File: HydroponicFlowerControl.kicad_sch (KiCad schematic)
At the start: 0 parts

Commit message: Add title to all schematics pages
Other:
- title: (none) -> RootMaster
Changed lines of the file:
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@@
 	(paper "A4")
 	(title_block
+		(title "RootMaster")
 		(rev "1")
 	)

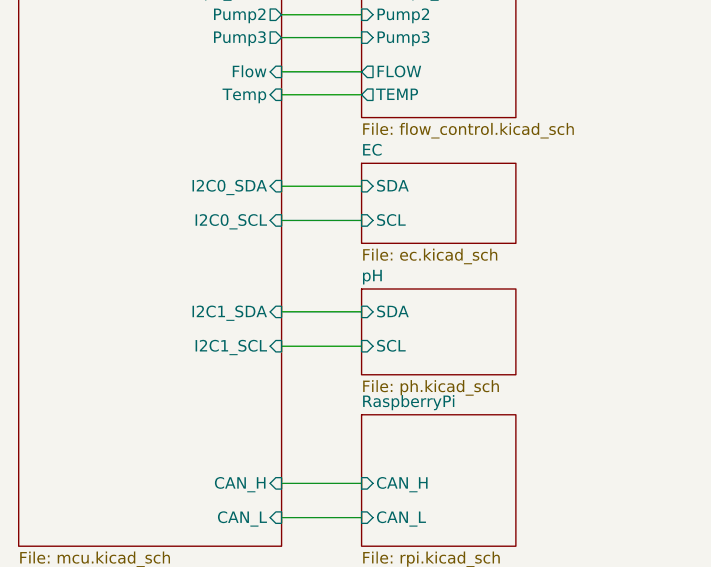
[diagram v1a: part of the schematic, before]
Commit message: Add disable signals for ec and ph
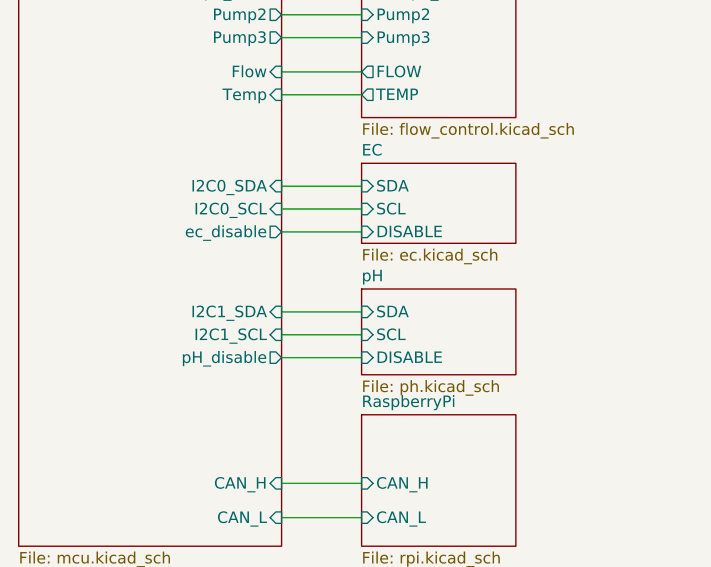
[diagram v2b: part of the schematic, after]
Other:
- sheet EC ports: added DISABLE; removed none
- sheet MCU ports: added ec_disable, pH_disable; removed none
- sheet pH ports: added DISABLE; removed none
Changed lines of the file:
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@@
-	(wire
-		(pts
-			(xy 49.53 154.94) (xy 58.42 154.94)
-		)
-		(stroke
-			(width 0)
-			(type default)
-		)
-	)
 	(wire
 		(pts
@@
 	(wire
 		(pts
-			(xy 49.53 140.97) (xy 58.42 140.97)
+			(xy 49.53 156.21) (xy 58.42 156.21)
+		)
+		(stroke
+			(width 0)
+			(type default)
+		)
+	)
+	(wire
+		(pts
+			(xy 49.53 139.7) (xy 58.42 139.7)
 		)
 		(stroke
@@
 	(wire
 		(pts
+			(xy 49.53 142.24) (xy 58.42 142.24)
+		)
+		(stroke
+			(width 0)
+			(type default)
+		)
+	)
+	(wire
+		(pts
 			(xy 109.22 41.91) (xy 116.84 41.91)
+		)
+		(stroke
+			(width 0)
+			(type default)
+		)
+	)
+	(wire
+		(pts
+			(xy 49.53 153.67) (xy 58.42 153.67)
 		)
 		(stroke
@@
 		)
 		(pin "SCL" input
-			(at 58.42 140.97 180)
+			(at 58.42 139.7 180)
 			(effects
 				(font
@@
 		(pin "SDA" input
 			(at 58.42 137.16 180)
+			(effects
+				(font
+					(size 1.27 1.27)
+				)
+				(justify left)
+			)
+		)
+		(pin "DISABLE" input
+			(at 58.42 142.24 180)
 			(effects
 				(font
@@
 		)
 		(pin "SCL" input
-			(at 58.42 154.94 180)
+			(at 58.42 153.67 180)
+			(effects
+				(font
+					(size 1.27 1.27)
+				)
+				(justify left)
+			)
+		)
+		(pin "DISABLE" input
+			(at 58.42 156.21 180)
 			(effects
 				(font
@@
 		)
 		(pin "I2C0_SCL" input
-			(at 49.53 140.97 0)
+			(at 49.53 139.7 0)
 			(effects
 				(font
@@
 		)
 		(pin "I2C1_SCL" input
-			(at 49.53 154.94 0)
+			(at 49.53 153.67 0)
 			(effects
 				(font
@@
 			(effects
 				(font
+					(size 1.27 1.27)
+				)
+				(justify right)
+			)
+		)
+		(pin "pH_disable" output
+			(at 49.53 156.21 0)
+			(effects
+				(font
+					(size 1.27 1.27)
+				)
+				(justify right)
+			)
+		)
+		(pin "ec_disable" output
+			(at 49.53 142.24 0)
+			(effects
+				(font

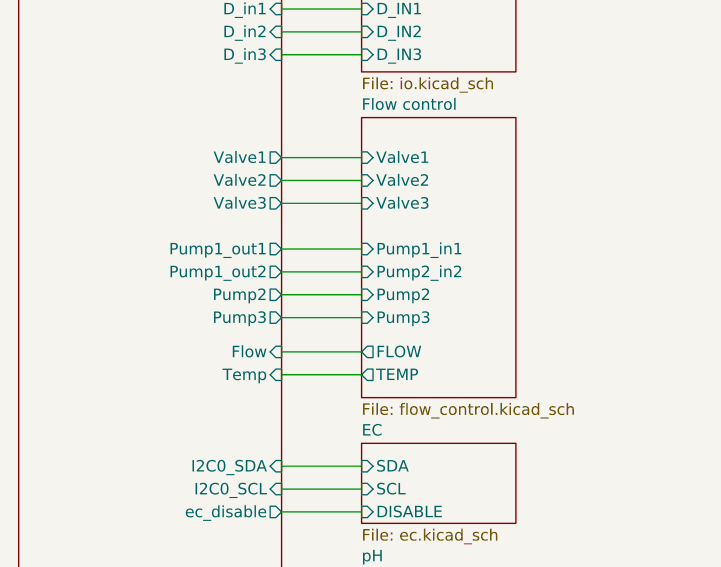
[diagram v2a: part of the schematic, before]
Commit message: Replace motor controller with mosfets instead
Closes #21
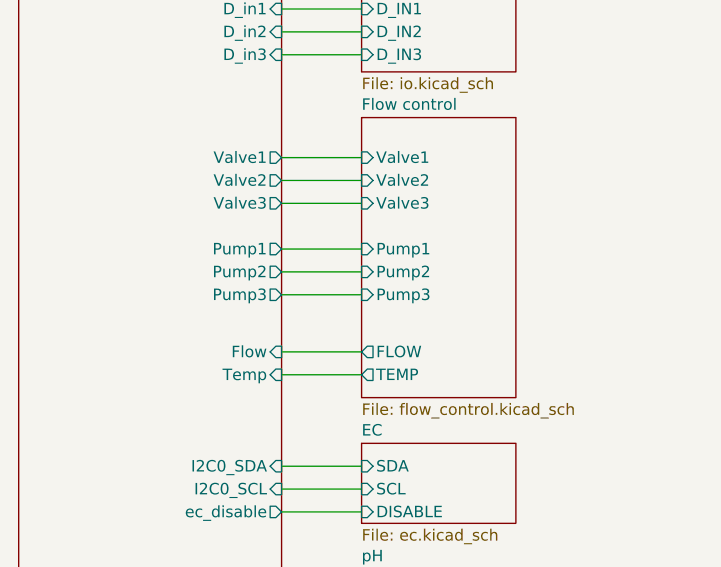
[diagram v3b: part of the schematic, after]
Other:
- sheet Flow control ports: added Pump1; removed Pump1_in1, Pump2_in2
- sheet MCU ports: added Pump1; removed Pump1_out1, Pump1_out2
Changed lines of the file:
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@@
+	(wire
+		(pts
+			(xy 49.53 115.57) (xy 58.42 115.57)
+		)
+		(stroke
+			(width 0)
+			(type default)
+		)
+	)
+	(wire
+		(pts
+			(xy 49.53 91.44) (xy 58.42 91.44)
+		)
+		(stroke
+			(width 0)
+			(type default)
+		)
+	)
+	(wire
+		(pts
+			(xy 49.53 107.95) (xy 58.42 107.95)
+		)
+		(stroke
+			(width 0)
+			(type default)
+		)
+	)
+	(wire
+		(pts
+			(xy 49.53 142.24) (xy 58.42 142.24)
+		)
+		(stroke
+			(width 0)
+			(type default)
+		)
+	)
+	(wire
+		(pts
+			(xy 109.22 41.91) (xy 116.84 41.91)
+		)
+		(stroke
+			(width 0)
+			(type default)
+		)
+	)
+	(wire
+		(pts
+			(xy 49.53 153.67) (xy 58.42 153.67)
+		)
+		(stroke
+			(width 0)
+			(type default)
+		)
+	)
 	(wire
 		(pts
@@
 	(wire
 		(pts
-			(xy 49.53 91.44) (xy 58.42 91.44)
-		)
-		(stroke
-			(width 0)
-			(type default)
-		)
-	)
-	(wire
-		(pts
-			(xy 49.53 107.95) (xy 58.42 107.95)
-		)
-		(stroke
-			(width 0)
-			(type default)
-		)
-	)
-	(wire
-		(pts
-			(xy 49.53 142.24) (xy 58.42 142.24)
-		)
-		(stroke
-			(width 0)
-			(type default)
-		)
-	)
-	(wire
-		(pts
-			(xy 109.22 41.91) (xy 116.84 41.91)
-		)
-		(stroke
-			(width 0)
-			(type default)
-		)
-	)
-	(wire
-		(pts
-			(xy 49.53 153.67) (xy 58.42 153.67)
-		)
-		(stroke
-			(width 0)
-			(type default)
-		)
-	)
-	(wire
-		(pts
-			(xy 49.53 120.65) (xy 58.42 120.65)
-		)
-		(stroke
-			(width 0)
-			(type default)
-		)
-	)
-	(wire
-		(pts
 			(xy 49.53 137.16) (xy 58.42 137.16)
 		)
@@
 		(pts
 			(xy 109.22 22.86) (xy 109.22 24.13)
-		)
-		(stroke
-			(width 0)
-			(type default)
-		)
-	)
-	(wire
-		(pts
-			(xy 49.53 115.57) (xy 58.42 115.57)
 		)
 		(stroke
@@
 		)
 		(pin "Pump3" input
-			(at 58.42 120.65 180)
+			(at 58.42 118.11 180)
 			(effects
 				(font
@@
 		)
 		(pin "Pump2" input
-			(at 58.42 118.11 180)
-			(effects
-				(font
-					(size 1.27 1.27)
-				)
-				(justify left)
-			)
-		)
-		(pin "Pump1_in1" input
+			(at 58.42 115.57 180)
+			(effects
+				(font
+					(size 1.27 1.27)
+				)
+				(justify left)
+			)
+		)
+		(pin "Pump1" input
 			(at 58.42 113.03 180)
-			(effects
-				(font
-					(size 1.27 1.27)
-				)
-				(justify left)
-			)
-		)
-		(pin "Pump2_in2" input
-			(at 58.42 115.57 180)
 			(effects
 				(font
@@
 			)
 		)
-		(pin "Pump1_out1" output
-			(at 49.53 113.03 0)
-			(effects
-				(font
-					(size 1.27 1.27)
-				)
-				(justify right)
-			)
-		)
-		(pin "Pump1_out2" output
+		(pin "Pump2" output
 			(at 49.53 115.57 0)
 			(effects
@@
 			)
 		)
-		(pin "Pump2" output
+		(pin "Pump3" output
 			(at 49.53 118.11 0)
-			(effects
-				(font
-					(size 1.27 1.27)
-				)
-				(justify right)
-			)
-		)
-		(pin "Pump3" output
-			(at 49.53 120.65 0)
 			(effects
 				(font
@@
 			(effects
 				(font
+					(size 1.27 1.27)
+				)
+				(justify right)
+			)
+		)
+		(pin "Pump1" output
+			(at 49.53 113.03 0)
+			(effects
+				(font

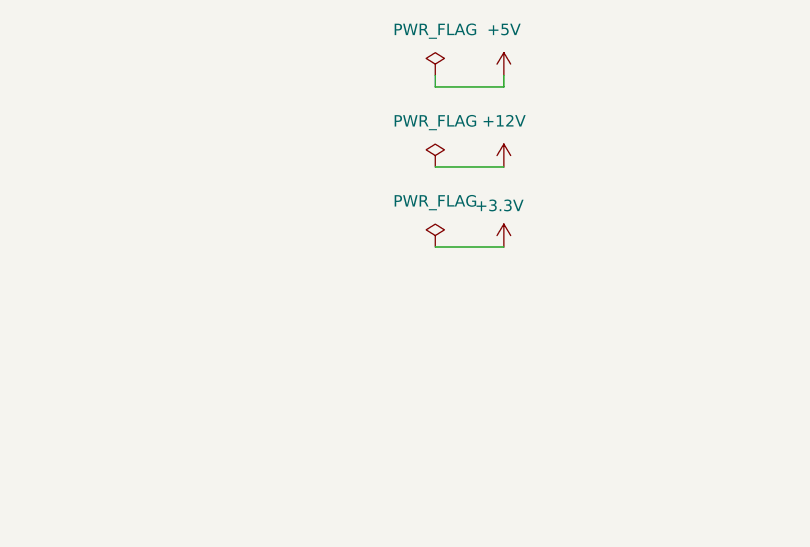
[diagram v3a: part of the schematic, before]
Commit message: Add testpoints for power and gnd
Closes #3
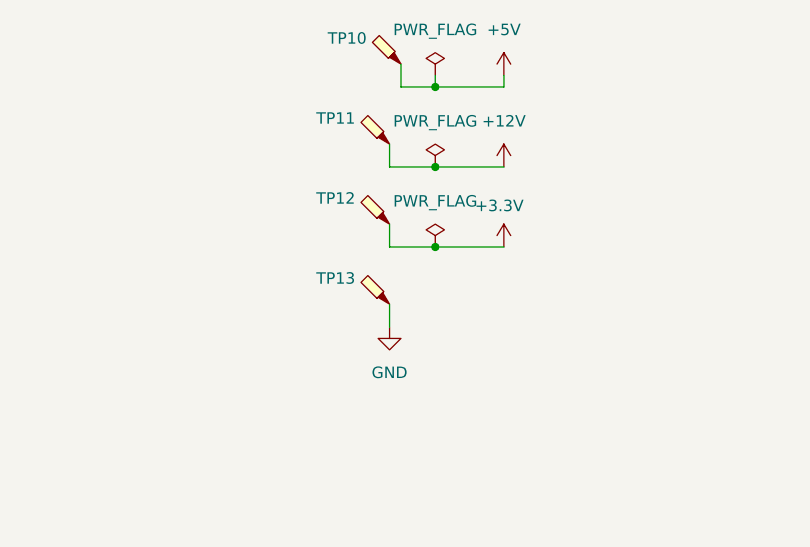
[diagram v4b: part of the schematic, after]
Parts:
- added TP10: 5V, TestPoint:TestPoint_Pad_D1.0mm, symbol Connector:TestPoint_Probe
- added TP11: 12V, TestPoint:TestPoint_Pad_D1.0mm, symbol Connector:TestPoint_Probe
- added TP12: 3.3V, TestPoint:TestPoint_Pad_D1.0mm, symbol Connector:TestPoint_Probe
- added TP13: GND, TestPoint:TestPoint_Loop_D1.80mm_Drill1.0mm_Beaded, symbol Connector:TestPoint_Probe
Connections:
- net +12V: now also TP11.1
- net +3.3V: now also TP12.1
- net +5V: now also TP10.1
- new net GND: TP13.1

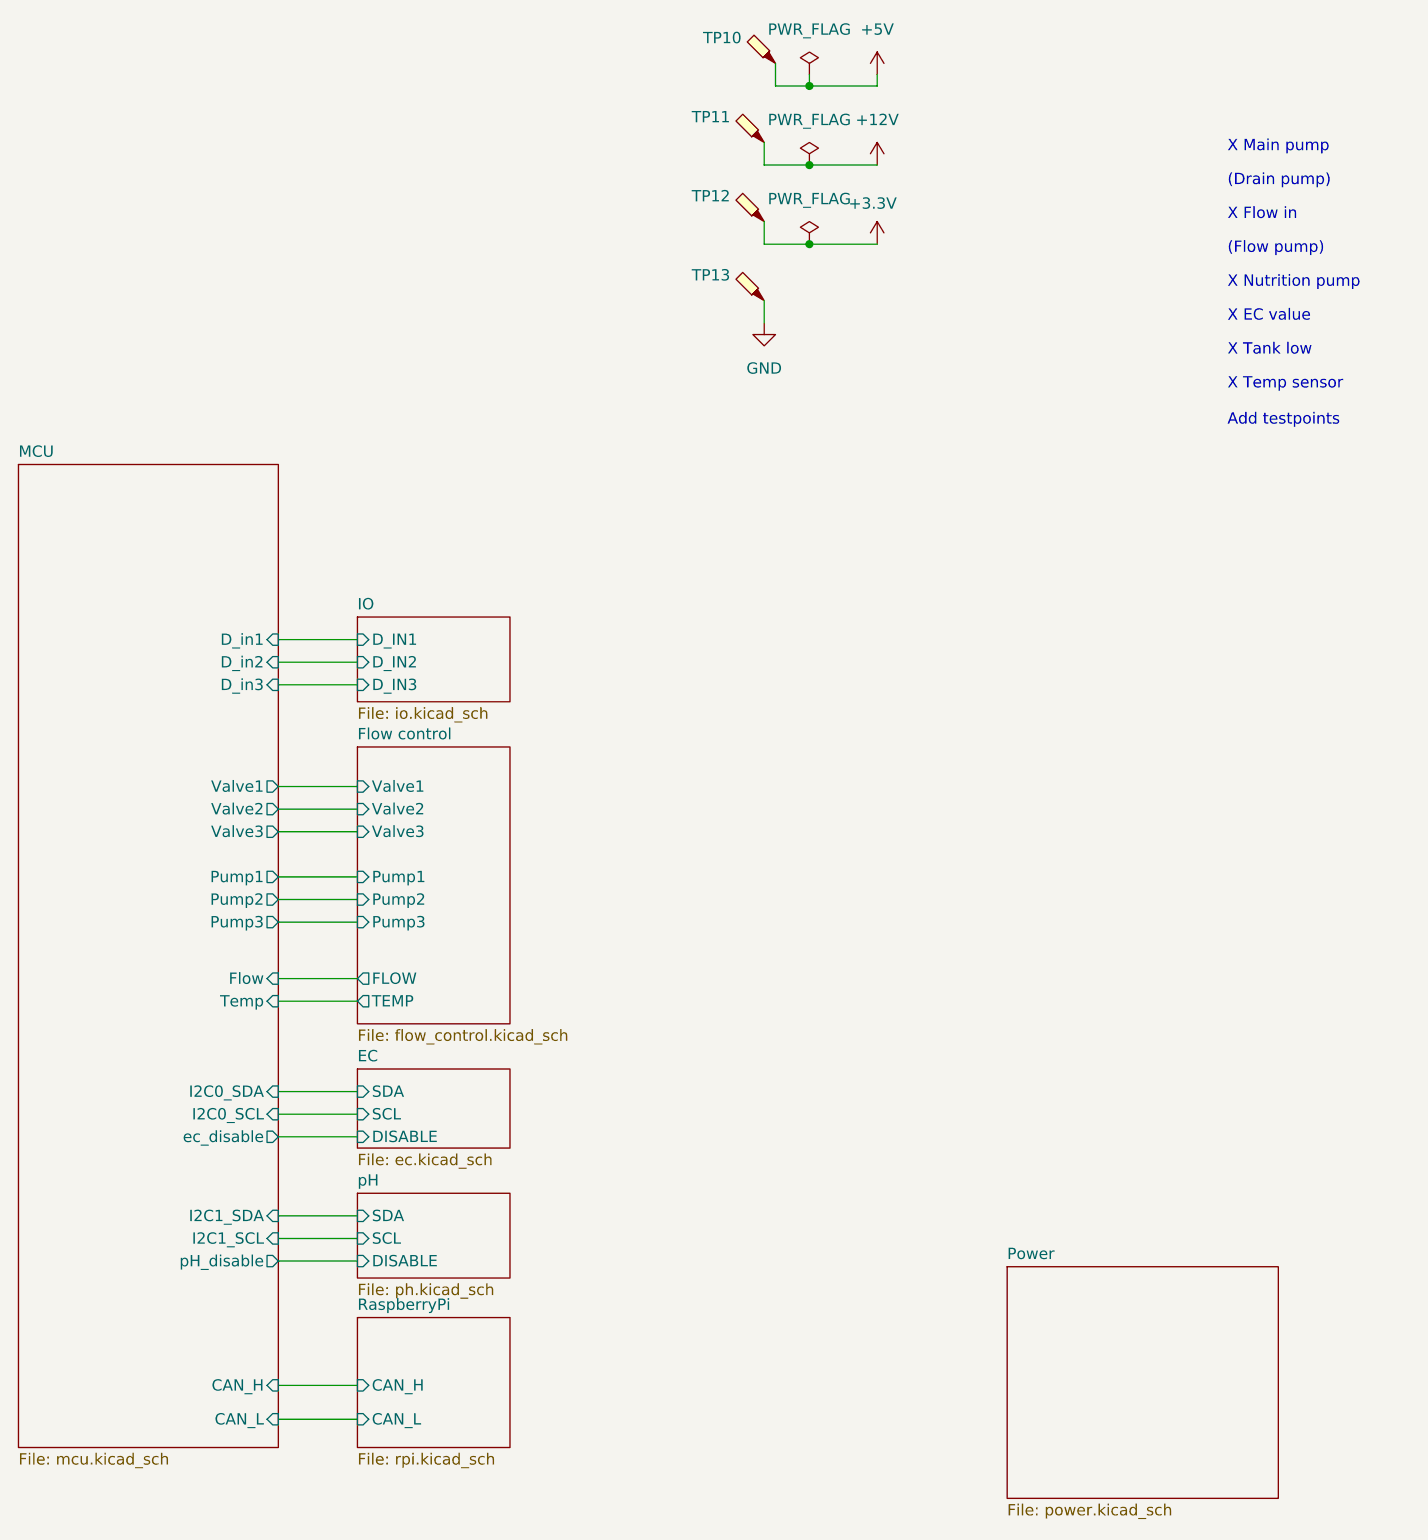
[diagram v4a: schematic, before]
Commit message: Route USB data signals to STM32
The CANbus needed to be moved together with ec and ph disable signals.
Closes #14 and #9
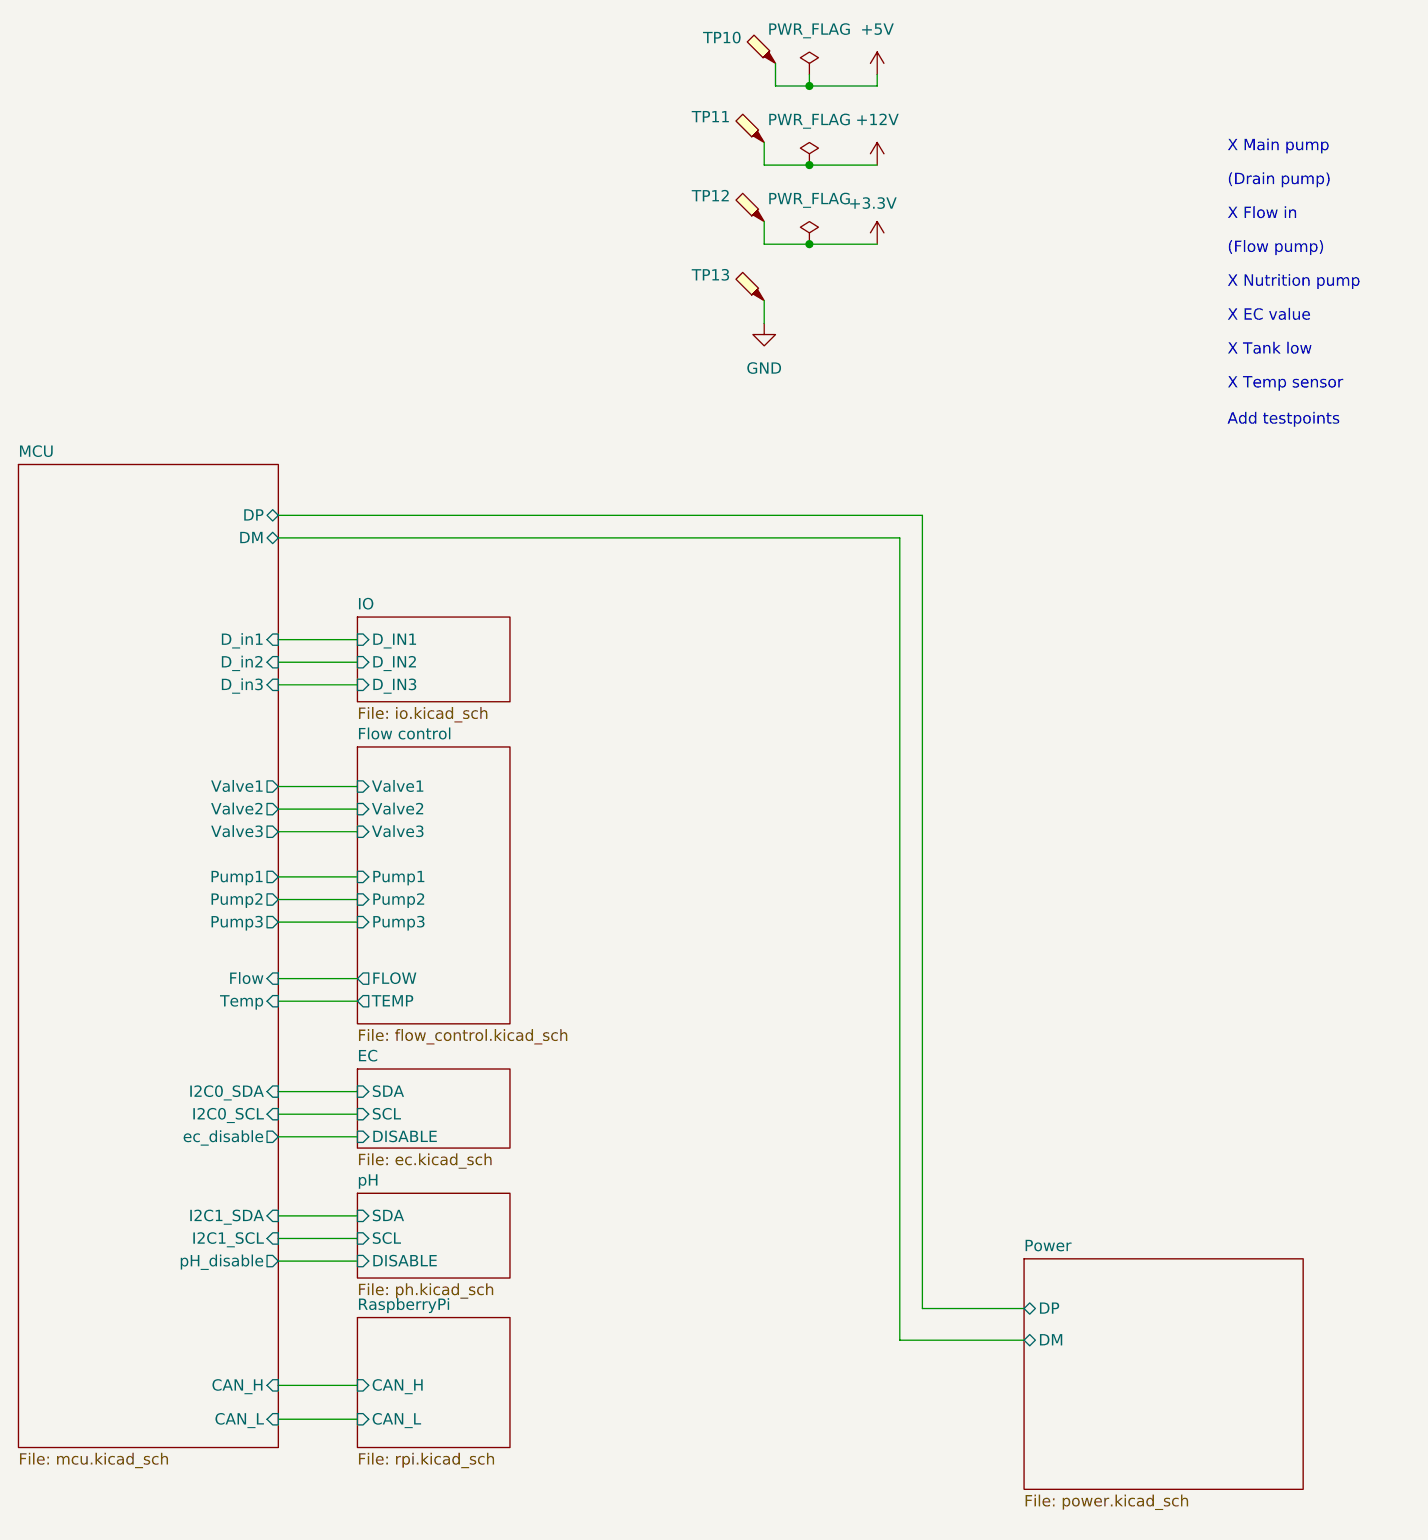
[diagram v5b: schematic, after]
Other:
- sheet MCU ports: added DM, DP; removed none
- sheet Power ports: added DM, DP; removed none
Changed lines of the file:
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@@
+	(wire
+		(pts
+			(xy 49.53 72.39) (xy 121.92 72.39)
+		)
+		(stroke
+			(width 0)
+			(type default)
+		)
+	)
+	(wire
+		(pts
+			(xy 121.92 72.39) (xy 121.92 161.544)
+		)
+		(stroke
+			(width 0)
+			(type default)
+		)
+	)
 	(wire
 		(pts
@@
 	(wire
 		(pts
+			(xy 121.92 161.544) (xy 133.35 161.544)
+		)
+		(stroke
+			(width 0)
+			(type default)
+		)
+	)
+	(wire
+		(pts
 			(xy 104.14 48.26) (xy 104.14 50.8)
 		)
@@
 	(wire
 		(pts
+			(xy 119.38 165.1) (xy 119.38 74.93)
+		)
+		(stroke
+			(width 0)
+			(type default)
+		)
+	)
+	(wire
+		(pts
 			(xy 104.14 41.91) (xy 109.22 41.91)
 		)
@@
 		(pts
 			(xy 109.22 24.13) (xy 116.84 24.13)
+		)
+		(stroke
+			(width 0)
+			(type default)
+		)
+	)
+	(wire
+		(pts
+			(xy 119.38 74.93) (xy 49.53 74.93)
+		)
+		(stroke
+			(width 0)
+			(type default)
+		)
+	)
+	(wire
+		(pts
+			(xy 133.35 165.1) (xy 119.38 165.1)
 		)
 		(stroke
@@
 	)
 	(sheet
-		(at 131.445 156.845)
-		(size 30.48 26.035)
+		(at 133.35 155.956)
+		(size 31.369 25.908)
 		(fields_autoplaced yes)
 		(stroke
@@
 		)
 		(property "Sheetname" "Power"
-			(at 131.445 156.1334 0)
+			(at 133.35 155.2444 0)
 			(effects
 				(font
@@
 		)
 		(property "Sheetfile" "power.kicad_sch"
-			(at 131.445 183.4646 0)
+			(at 133.35 182.4486 0)
 			(effects
 				(font
@@
 				)
 				(justify left top)
+			)
+		)
+		(pin "DP" bidirectional
+			(at 133.35 161.544 180)
+			(effects
+				(font
+					(size 1.27 1.27)
+				)
+				(justify left)
+			)
+		)
+		(pin "DM" bidirectional
+			(at 133.35 165.1 180)
+			(effects
+				(font
+					(size 1.27 1.27)
+				)
+				(justify left)
 			)
 		)
@@
 			(effects
 				(font
+					(size 1.27 1.27)
+				)
+				(justify right)
+			)
+		)
+		(pin "DP" bidirectional
+			(at 49.53 72.39 0)
+			(effects
+				(font
+					(size 1.27 1.27)
+				)
+				(justify right)
+			)
+		)
+		(pin "DM" bidirectional
+			(at 49.53 74.93 0)
+			(effects
+				(font
